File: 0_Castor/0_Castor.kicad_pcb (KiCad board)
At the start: 2 copper layers, 135.3 x 173.4 mm, 131 parts, among them U1 Nice_Nano_V2, U2 RT9701, U3 AP9101CK

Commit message: feat: add controller, battery jack, battery switch and reset switch placement
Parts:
- removed U2: RT9701, Package_TO_SOT_SMD:TO-252-4
- removed U3: AP9101CK, Package_TO_SOT_SMD:SOT-23-5
- added J1: Conn_01x02, Connector_JST:JST_PH_S2B-PH-K_1x02_P2.00mm_Horizontal, F.Cu at (135.5, 54.8)
- added R1: Resistor, ScottoKeebs_Components:Resistor_0402, F.Cu at (167.2, 125.9)
- added R2: Resistor, ScottoKeebs_Components:Resistor_0402, F.Cu at (51.9, 62.7)
- added R3: Resistor, ScottoKeebs_Components:Resistor_0402, F.Cu at (51.8, 119.8)
- added R4: Resistor, ScottoKeebs_Components:Resistor_0402, F.Cu at (156.8, 195.2)
- added SW1: Reset Switch, Button_Switch_SMD:Panasonic_EVQPUL_EVQPUC, F.Cu at (168.6, 157.4)
- added SW2: Battery Switch, footprints:SPDT_C128955, B.Cu at (170.1, 72.1)
- U1: moved to B.Cu
- moved U1 201.1 mm to (153.7, 45.3), turned to 90 degrees
- moved D63 4.58 mm to (129.2, 44.0)
- moved LED41 0.87 mm to (119.5, 166.2)
- moved S69 0.87 mm to (115.8, 180.0)
- moved LED44 0.87 mm to (151.4, 194.5)
- moved D68 0.87 mm to (128.1, 163.6)
- moved D69 0.87 mm to (123.2, 182.0)
- moved D76 0.87 mm to (146.5, 168.5)
- moved D77 0.87 mm to (141.6, 186.9)
- moved S68 0.87 mm to (120.7, 161.6)
- moved S77 0.87 mm to (134.2, 185.0)
- moved LED42 0.87 mm to (114.6, 184.6)
- moved LED43 0.87 mm to (133.0, 189.6)
- moved D83 0.87 mm to (164.9, 173.5)
- moved LED40 0.87 mm to (137.9, 171.2)
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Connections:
- LED1 pad 2: /LEDs/VSS -> /GND
- LED1 pad 3: /LED DIN0 -> Net-(LED1-DIN)
- LED1 pad 4: /LEDs/VDD -> /RAW
- LED10 pad 2: /LEDs/VSS -> /GND
- LED10 pad 4: /LEDs/VDD -> /RAW
- LED11 pad 2: /LEDs/VSS -> /GND
- LED11 pad 4: /LEDs/VDD -> /RAW
- LED12 pad 2: /LEDs/VSS -> /GND
- LED12 pad 4: /LEDs/VDD -> /RAW
- LED13 pad 2: /LEDs/VSS -> /GND
- LED13 pad 4: /LEDs/VDD -> /RAW
- LED14 pad 2: /LEDs/VSS -> /GND
- LED14 pad 4: /LEDs/VDD -> /RAW
- LED15 pad 2: /LEDs/VSS -> /GND
- LED15 pad 4: /LEDs/VDD -> /RAW
- LED16 pad 2: /LEDs/VSS -> /GND
- LED16 pad 4: /LEDs/VDD -> /RAW
- LED17 pad 2: /LEDs/VSS -> /GND
- LED17 pad 4: /LEDs/VDD -> /RAW
- LED18 pad 2: /LEDs/VSS -> /GND
- LED18 pad 4: /LEDs/VDD -> /RAW
- LED19 pad 2: /LEDs/VSS -> /GND
- LED19 pad 4: /LEDs/VDD -> /RAW
- LED2 pad 2: /LEDs/VSS -> /GND
- LED2 pad 4: /LEDs/VDD -> /RAW
- LED20 pad 2: /LEDs/VSS -> /GND
- LED20 pad 4: /LEDs/VDD -> /RAW
- LED21 pad 2: /LEDs/VSS -> /GND
- LED21 pad 4: /LEDs/VDD -> /RAW
- LED22 pad 2: /LEDs/VSS -> /GND
- LED22 pad 4: /LEDs/VDD -> /RAW
- LED23 pad 2: /LEDs/VSS -> /GND
- LED23 pad 4: /LEDs/VDD -> /RAW
- LED24 pad 2: /LEDs/VSS -> /GND
- LED24 pad 4: /LEDs/VDD -> /RAW
- LED25 pad 1: unconnected-(LED25-DOUT-Pad1) -> Net-(LED25-DOUT)
- LED25 pad 2: /LEDs/VSS -> /GND
- LED25 pad 4: /LEDs/VDD -> /RAW
- LED26 pad 2: /LEDs/VSS -> /GND
- LED26 pad 3: /LED DIN1 -> Net-(LED26-DIN)
- LED26 pad 4: /LEDs/VDD -> /RAW
- LED27 pad 2: /LEDs/VSS -> /GND
- LED27 pad 4: /LEDs/VDD -> /RAW
- LED28 pad 2: /LEDs/VSS -> /GND
- LED28 pad 4: /LEDs/VDD -> /RAW
- LED29 pad 2: /LEDs/VSS -> /GND
- LED29 pad 4: /LEDs/VDD -> /RAW
- LED3 pad 2: /LEDs/VSS -> /GND
- LED3 pad 4: /LEDs/VDD -> /RAW
- LED30 pad 2: /LEDs/VSS -> /GND
- LED30 pad 4: /LEDs/VDD -> /RAW
- LED31 pad 2: /LEDs/VSS -> /GND
- LED31 pad 4: /LEDs/VDD -> /RAW
- LED32 pad 2: /LEDs/VSS -> /GND
- LED32 pad 4: /LEDs/VDD -> /RAW
- LED33 pad 2: /LEDs/VSS -> /GND
- LED33 pad 4: /LEDs/VDD -> /RAW
- LED34 pad 2: /LEDs/VSS -> /GND
- LED34 pad 4: /LEDs/VDD -> /RAW
- LED35 pad 2: /LEDs/VSS -> /GND
- LED35 pad 4: /LEDs/VDD -> /RAW
- LED36 pad 2: /LEDs/VSS -> /GND
- LED36 pad 4: /LEDs/VDD -> /RAW
- LED37 pad 2: /LEDs/VSS -> /GND
- LED37 pad 4: /LEDs/VDD -> /RAW
- LED38 pad 2: /LEDs/VSS -> /GND
- LED38 pad 4: /LEDs/VDD -> /RAW
- LED39 pad 2: /LEDs/VSS -> /GND
- LED39 pad 4: /LEDs/VDD -> /RAW
- LED4 pad 2: /LEDs/VSS -> /GND
- LED4 pad 4: /LEDs/VDD -> /RAW
- LED40 pad 2: /LEDs/VSS -> /GND
- LED40 pad 4: /LEDs/VDD -> /RAW
- LED41 pad 2: /LEDs/VSS -> /GND
- LED41 pad 4: /LEDs/VDD -> /RAW
- LED42 pad 2: /LEDs/VSS -> /GND
- LED42 pad 4: /LEDs/VDD -> /RAW
- LED43 pad 2: /LEDs/VSS -> /GND
- LED43 pad 4: /LEDs/VDD -> /RAW
- LED44 pad 1: unconnected-(LED44-DOUT-Pad1) -> Net-(LED44-DOUT)
- LED44 pad 2: /LEDs/VSS -> /GND
- LED44 pad 4: /LEDs/VDD -> /RAW
- LED5 pad 2: /LEDs/VSS -> /GND
- LED5 pad 4: /LEDs/VDD -> /RAW
- LED6 pad 2: /LEDs/VSS -> /GND
- LED6 pad 4: /LEDs/VDD -> /RAW
- LED7 pad 2: /LEDs/VSS -> /GND
- LED7 pad 4: /LEDs/VDD -> /RAW
- LED8 pad 2: /LEDs/VSS -> /GND
- LED8 pad 4: /LEDs/VDD -> /RAW
- LED9 pad 2: /LEDs/VSS -> /GND
- LED9 pad 4: /LEDs/VDD -> /RAW
- U1 pad 22: unconnected-(U1-RST-Pad22) -> /RST
- U1 pad 23: unconnected-(U1-GND-Pad23) -> /GND
- U1 pad 24: unconnected-(U1-B+-Pad24) -> /RAW
- U1 pad 3: unconnected-(U1-GND-Pad3) -> /GND
- U1 pad 4: unconnected-(U1-GND-Pad4) -> /GND
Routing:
- net Net-(LED38-DOUT): track 36.9 -> 0.00 mm
- net Net-(LED31-DOUT): track 34.9 -> 0.00 mm
- net Net-(LED13-DOUT): track 26.5 -> 0.00 mm
- net Net-(LED41-DOUT): track 24.7 -> 0.00 mm
- net Net-(LED30-DOUT): track 23.7 -> 0.00 mm
- net Net-(LED24-DOUT): track 23.7 -> 0.00 mm
- net Net-(LED14-DOUT): track 23.7 -> 0.00 mm
- net Net-(LED1-DOUT): track 23.7 -> 0.00 mm
- net Net-(LED6-DOUT): track 23.1 -> 0.00 mm
- net Net-(LED19-DOUT): track 22.8 -> 0.00 mm
- net Net-(LED29-DOUT): track 16.9 -> 0.00 mm
- net Net-(LED23-DOUT): track 16.9 -> 0.00 mm
- net Net-(LED15-DOUT): track 16.9 -> 0.00 mm
- net Net-(LED10-DOUT): track 16.9 -> 0.00 mm
- net Net-(LED34-DOUT): track 16.9 -> 0.00 mm
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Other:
- board size 135.3 x 173.4 mm -> 135.3 x 172.8 mm
- board text removed: "Needs to be placed properly (sub-millimeter precision)"

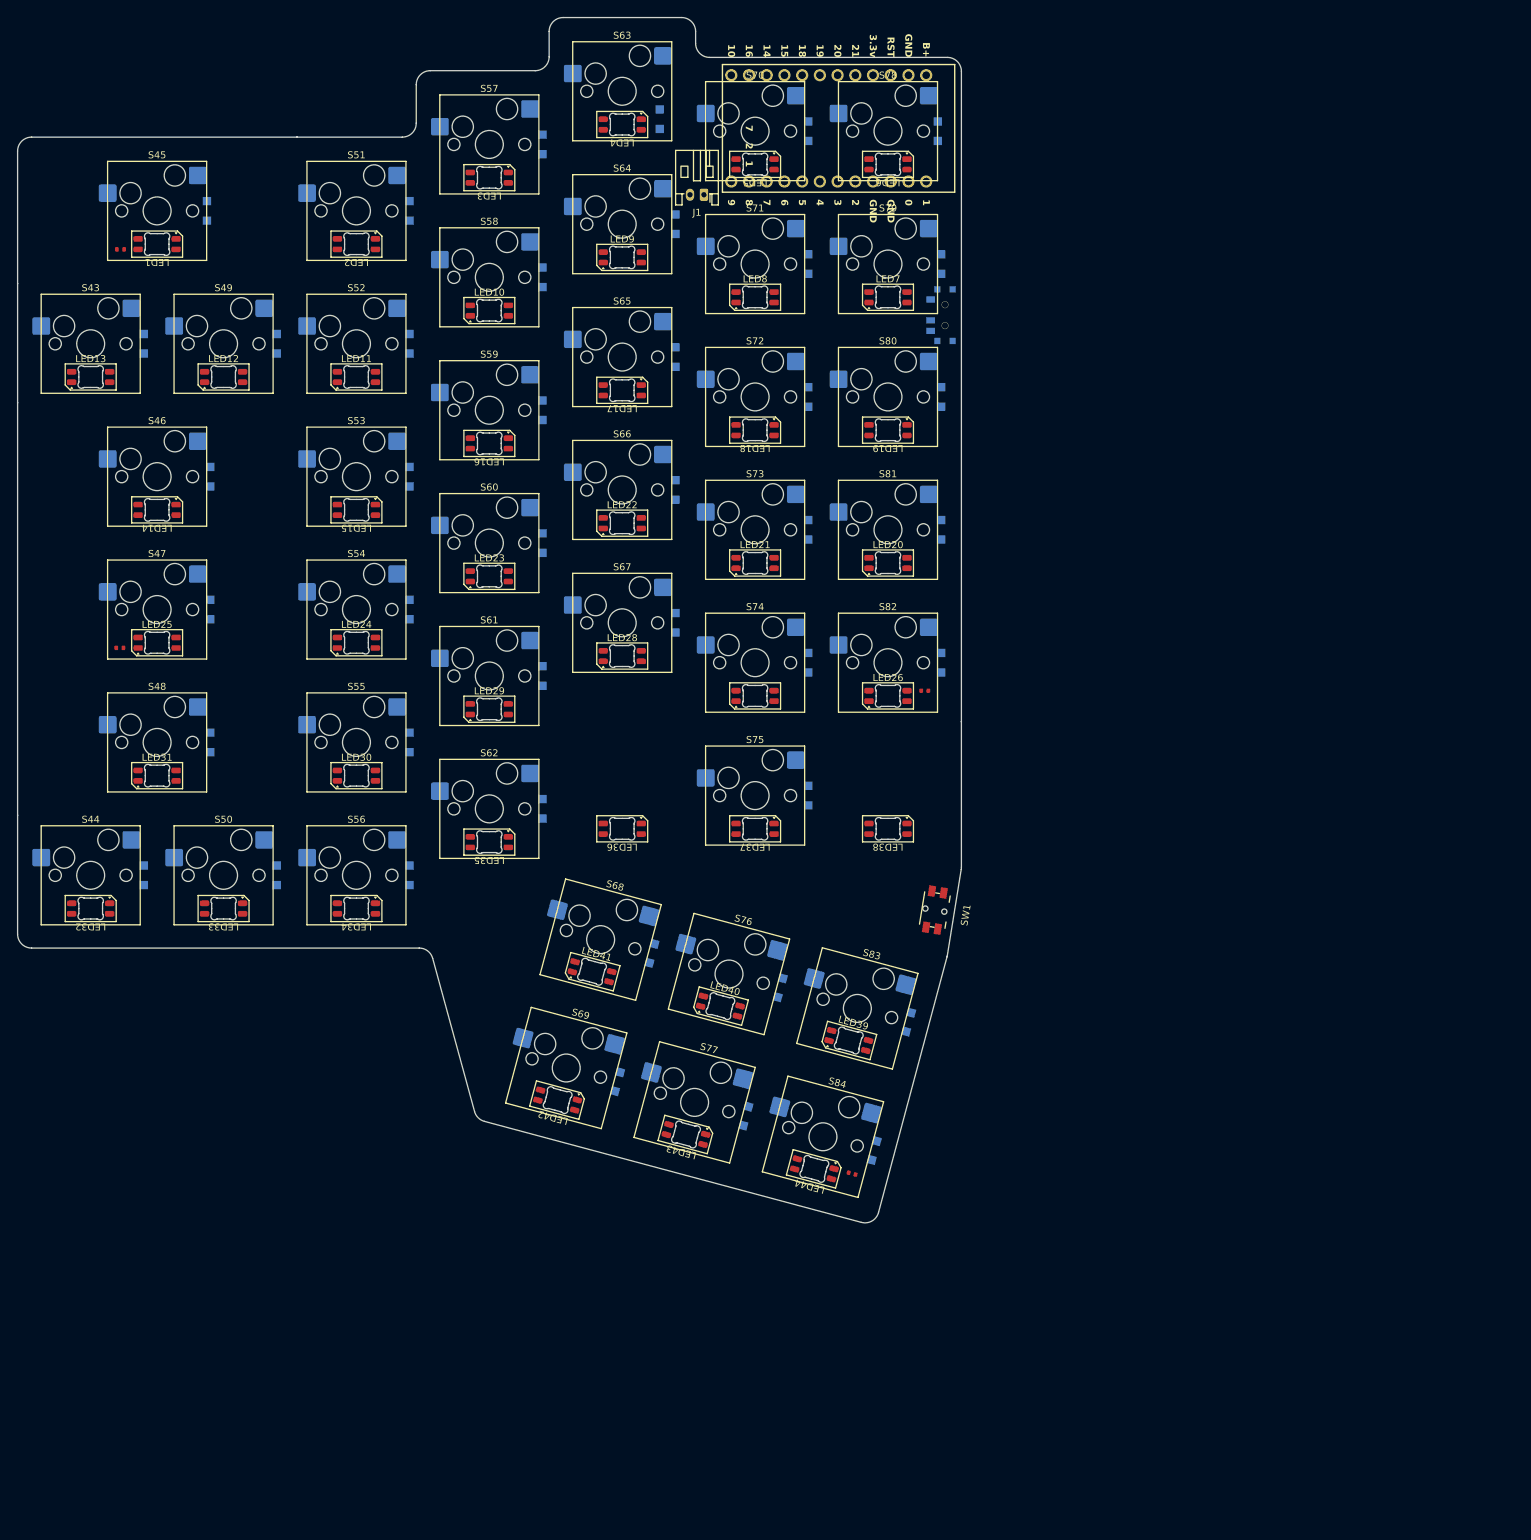
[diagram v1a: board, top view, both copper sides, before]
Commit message: feat: add LEDs, capacitors, resistors and rework schematic
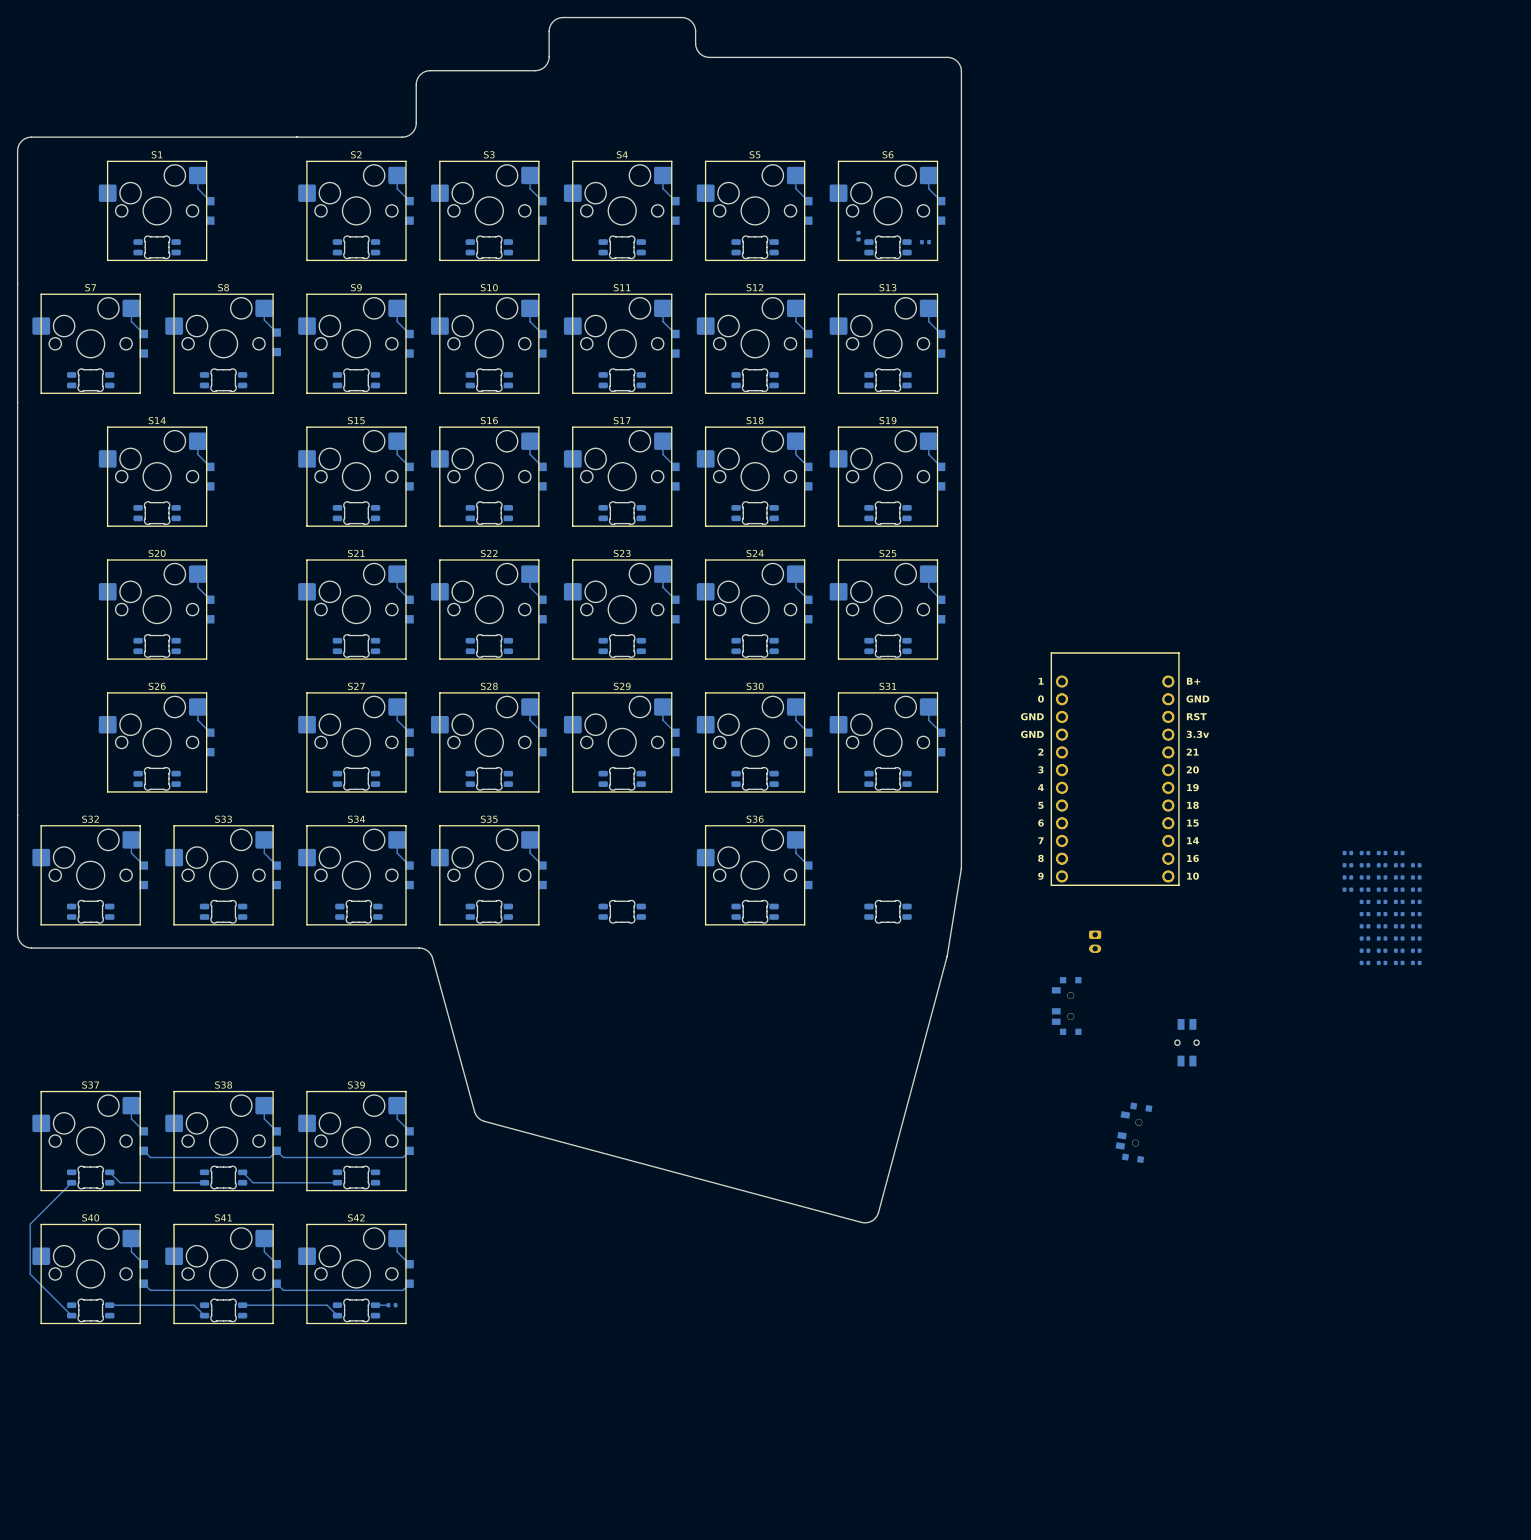
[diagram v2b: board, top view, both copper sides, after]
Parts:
- removed D43, D44, D45, D46, D47, D48, D49, D50, D51, D52, D53, D54, D55, D56, D57, D58, D59, D60, D61, D62, D63, D64, D65, D66, D67, D68, D69, D70, D71, D72, D73, D74, D75, D76, D77, D78, D79, D80, D81, D82, D83, D84: ~, Diode_SMD:Nexperia_CFP3_SOD-123W
- removed R3, R4: Resistor, ScottoKeebs_Components:Resistor_0402
- removed S43, S44, S49, S50, S51, S52, S53, S54, S55, S56, S57, S58, S59, S60, S61, S62, S63, S64, S65, S66, S67, S68, S69, S70, S71, S72, S73, S74, S76, S77, S78, S79, S80, S81, S82, S83, S84: ~, ScottoKeebs_Hotswap:Hotswap_MX_1.00u
- removed S45, S46, S47, S48: ~, ScottoKeebs_Hotswap:Hotswap_MX_2.00u
- removed S75: ~, ScottoKeebs_Hotswap:Hotswap_MX_3.00u
- added C1: 100nF, Capacitor_SMD:C_0402_1005Metric, B.Cu at (157.7, 60.8)
- added C10: 100nF, Capacitor_SMD:C_0402_1005Metric, B.Cu at (237.7, 165.0)
- added C11: 100nF, Capacitor_SMD:C_0402_1005Metric, B.Cu at (235.2, 149.2)
- added C12: 100nF, Capacitor_SMD:C_0402_1005Metric, B.Cu at (235.2, 151.0)
- added C13: 100nF, Capacitor_SMD:C_0402_1005Metric, B.Cu at (235.2, 152.7)
- added C14: 100nF, Capacitor_SMD:C_0402_1005Metric, B.Cu at (235.2, 154.5)
- added C15: 100nF, Capacitor_SMD:C_0402_1005Metric, B.Cu at (235.2, 156.2)
- added C16: 100nF, Capacitor_SMD:C_0402_1005Metric, B.Cu at (235.2, 158.0)
- added C17: 100nF, Capacitor_SMD:C_0402_1005Metric, B.Cu at (235.2, 159.7)
- added C18: 100nF, Capacitor_SMD:C_0402_1005Metric, B.Cu at (235.2, 161.5)
- added C19: 100nF, Capacitor_SMD:C_0402_1005Metric, B.Cu at (235.2, 163.2)
- added C2: 100nF, Capacitor_SMD:C_0402_1005Metric, B.Cu at (237.7, 151.0)
- added C20: 100nF, Capacitor_SMD:C_0402_1005Metric, B.Cu at (235.2, 165.0)
- added C21: 100nF, Capacitor_SMD:C_0402_1005Metric, B.Cu at (232.8, 149.2)
- added C22: 100nF, Capacitor_SMD:C_0402_1005Metric, B.Cu at (232.8, 151.0)
- added C23: 100nF, Capacitor_SMD:C_0402_1005Metric, B.Cu at (232.8, 152.7)
- added C24: 100nF, Capacitor_SMD:C_0402_1005Metric, B.Cu at (232.8, 154.5)
- added C25: 100nF, Capacitor_SMD:C_0402_1005Metric, B.Cu at (232.8, 156.2)
- added C26: 100nF, Capacitor_SMD:C_0402_1005Metric, B.Cu at (232.8, 158.0)
- added C27: 100nF, Capacitor_SMD:C_0402_1005Metric, B.Cu at (232.8, 159.7)
- added C28: 100nF, Capacitor_SMD:C_0402_1005Metric, B.Cu at (232.8, 161.5)
- added C29: 100nF, Capacitor_SMD:C_0402_1005Metric, B.Cu at (232.8, 163.2)
- added C3: 100nF, Capacitor_SMD:C_0402_1005Metric, B.Cu at (237.7, 152.7)
- added C30: 100nF, Capacitor_SMD:C_0402_1005Metric, B.Cu at (232.8, 165.0)
- added C31: 100nF, Capacitor_SMD:C_0402_1005Metric, B.Cu at (230.3, 149.2)
- added C32: 100nF, Capacitor_SMD:C_0402_1005Metric, B.Cu at (230.3, 151.0)
- added C33: 100nF, Capacitor_SMD:C_0402_1005Metric, B.Cu at (230.3, 152.7)
- added C34: 100nF, Capacitor_SMD:C_0402_1005Metric, B.Cu at (230.3, 154.5)
- added C35: 100nF, Capacitor_SMD:C_0402_1005Metric, B.Cu at (230.3, 156.2)
- added C36: 100nF, Capacitor_SMD:C_0402_1005Metric, B.Cu at (230.3, 158.0)
- added C37: 100nF, Capacitor_SMD:C_0402_1005Metric, B.Cu at (230.3, 159.7)
- added C38: 100nF, Capacitor_SMD:C_0402_1005Metric, B.Cu at (230.3, 161.5)
- added C39: 100nF, Capacitor_SMD:C_0402_1005Metric, B.Cu at (230.3, 163.2)
- added C4: 100nF, Capacitor_SMD:C_0402_1005Metric, B.Cu at (237.7, 154.5)
- added C40: 100nF, Capacitor_SMD:C_0402_1005Metric, B.Cu at (230.3, 165.0)
- added C41: 100nF, Capacitor_SMD:C_0402_1005Metric, B.Cu at (227.9, 149.2)
- added C42: 100nF, Capacitor_SMD:C_0402_1005Metric, B.Cu at (227.9, 151.0)
- added C43: 100nF, Capacitor_SMD:C_0402_1005Metric, B.Cu at (227.9, 152.7)
- added C44: 100nF, Capacitor_SMD:C_0402_1005Metric, B.Cu at (227.9, 154.5)
- added C5: 100nF, Capacitor_SMD:C_0402_1005Metric, B.Cu at (237.7, 156.2)
- added C6: 100nF, Capacitor_SMD:C_0402_1005Metric, B.Cu at (237.7, 158.0)
- added C7: 100nF, Capacitor_SMD:C_0402_1005Metric, B.Cu at (237.7, 159.7)
- added C8: 100nF, Capacitor_SMD:C_0402_1005Metric, B.Cu at (237.7, 161.5)
- added C9: 100nF, Capacitor_SMD:C_0402_1005Metric, B.Cu at (237.7, 163.2)
- added D1: ~, Diode_SMD:Nexperia_CFP3_SOD-123W, B.Cu at (64.8, 57.1)
- added D10: ~, Diode_SMD:Nexperia_CFP3_SOD-123W, B.Cu at (112.4, 76.2)
- added D11: ~, Diode_SMD:Nexperia_CFP3_SOD-123W, B.Cu at (131.4, 76.2)
- added D12: ~, Diode_SMD:Nexperia_CFP3_SOD-123W, B.Cu at (150.5, 76.2)
- added D13: ~, Diode_SMD:Nexperia_CFP3_SOD-123W, B.Cu at (169.5, 76.2)
- added D14: ~, Diode_SMD:Nexperia_CFP3_SOD-123W, B.Cu at (64.8, 95.2)
- added D15: ~, Diode_SMD:Nexperia_CFP3_SOD-123W, B.Cu at (93.3, 95.2)
- added D16: ~, Diode_SMD:Nexperia_CFP3_SOD-123W, B.Cu at (112.4, 95.2)
- added D17: ~, Diode_SMD:Nexperia_CFP3_SOD-123W, B.Cu at (131.4, 95.2)
- added D18: ~, Diode_SMD:Nexperia_CFP3_SOD-123W, B.Cu at (150.5, 95.2)
- added D19: ~, Diode_SMD:Nexperia_CFP3_SOD-123W, B.Cu at (169.5, 95.2)
- added D2: ~, Diode_SMD:Nexperia_CFP3_SOD-123W, B.Cu at (93.3, 57.1)
- added D20: ~, Diode_SMD:Nexperia_CFP3_SOD-123W, B.Cu at (64.8, 114.3)
- added D21: ~, Diode_SMD:Nexperia_CFP3_SOD-123W, B.Cu at (93.3, 114.3)
- added D22: ~, Diode_SMD:Nexperia_CFP3_SOD-123W, B.Cu at (112.4, 114.3)
- added D23: ~, Diode_SMD:Nexperia_CFP3_SOD-123W, B.Cu at (131.4, 114.3)
- added D24: ~, Diode_SMD:Nexperia_CFP3_SOD-123W, B.Cu at (150.5, 114.3)
- added D25: ~, Diode_SMD:Nexperia_CFP3_SOD-123W, B.Cu at (169.5, 114.3)
- added D26: ~, Diode_SMD:Nexperia_CFP3_SOD-123W, B.Cu at (64.8, 133.3)
- added D27: ~, Diode_SMD:Nexperia_CFP3_SOD-123W, B.Cu at (93.3, 133.3)
- added D28: ~, Diode_SMD:Nexperia_CFP3_SOD-123W, B.Cu at (112.4, 133.3)
- added D29: ~, Diode_SMD:Nexperia_CFP3_SOD-123W, B.Cu at (131.4, 133.3)
- added D3: ~, Diode_SMD:Nexperia_CFP3_SOD-123W, B.Cu at (112.4, 57.1)
- added D30: ~, Diode_SMD:Nexperia_CFP3_SOD-123W, B.Cu at (150.5, 133.3)
- added D31: ~, Diode_SMD:Nexperia_CFP3_SOD-123W, B.Cu at (169.5, 133.3)
- added D32: ~, Diode_SMD:Nexperia_CFP3_SOD-123W, B.Cu at (55.2, 152.4)
- added D33: ~, Diode_SMD:Nexperia_CFP3_SOD-123W, B.Cu at (74.3, 152.4)
- added D34: ~, Diode_SMD:Nexperia_CFP3_SOD-123W, B.Cu at (93.3, 152.4)
- added D35: ~, Diode_SMD:Nexperia_CFP3_SOD-123W, B.Cu at (112.4, 152.4)
- added D36: ~, Diode_SMD:Nexperia_CFP3_SOD-123W, B.Cu at (150.5, 152.4)
- added D37: ~, Diode_SMD:Nexperia_CFP3_SOD-123W, B.Cu at (55.2, 190.5)
- added D38: ~, Diode_SMD:Nexperia_CFP3_SOD-123W, B.Cu at (74.3, 190.5)
- added D39: ~, Diode_SMD:Nexperia_CFP3_SOD-123W, B.Cu at (93.3, 190.5)
- added D4: ~, Diode_SMD:Nexperia_CFP3_SOD-123W, B.Cu at (131.4, 57.1)
- added D40: ~, Diode_SMD:Nexperia_CFP3_SOD-123W, B.Cu at (55.2, 209.6)
- added D41: ~, Diode_SMD:Nexperia_CFP3_SOD-123W, B.Cu at (74.3, 209.6)
- added D42: ~, Diode_SMD:Nexperia_CFP3_SOD-123W, B.Cu at (93.3, 209.6)
- added D5: ~, Diode_SMD:Nexperia_CFP3_SOD-123W, B.Cu at (150.5, 57.1)
- added D6: ~, Diode_SMD:Nexperia_CFP3_SOD-123W, B.Cu at (169.5, 57.1)
- added D7: ~, Diode_SMD:Nexperia_CFP3_SOD-123W, B.Cu at (55.2, 76.2)
- added D8: ~, Diode_SMD:Nexperia_CFP3_SOD-123W, B.Cu at (74.3, 76.0)
- added D9: ~, Diode_SMD:Nexperia_CFP3_SOD-123W, B.Cu at (93.3, 76.2)
- added S1: ~, ScottoKeebs_Hotswap:Hotswap_MX_2.00u, F.Cu at (57.1, 57.1)
- added S10: ~, ScottoKeebs_Hotswap:Hotswap_MX_1.00u, F.Cu at (104.8, 76.2)
- added S11: ~, ScottoKeebs_Hotswap:Hotswap_MX_1.00u, F.Cu at (123.8, 76.2)
- added S12: ~, ScottoKeebs_Hotswap:Hotswap_MX_1.00u, F.Cu at (142.9, 76.2)
- added S13: ~, ScottoKeebs_Hotswap:Hotswap_MX_1.00u, F.Cu at (161.9, 76.2)
- added S14: ~, ScottoKeebs_Hotswap:Hotswap_MX_2.00u, F.Cu at (57.1, 95.2)
- added S15: ~, ScottoKeebs_Hotswap:Hotswap_MX_1.00u, F.Cu at (85.7, 95.2)
- added S16: ~, ScottoKeebs_Hotswap:Hotswap_MX_1.00u, F.Cu at (104.8, 95.2)
- added S17: ~, ScottoKeebs_Hotswap:Hotswap_MX_1.00u, F.Cu at (123.8, 95.2)
- added S18: ~, ScottoKeebs_Hotswap:Hotswap_MX_1.00u, F.Cu at (142.9, 95.2)
- added S19: ~, ScottoKeebs_Hotswap:Hotswap_MX_1.00u, F.Cu at (161.9, 95.2)
- added S2: ~, ScottoKeebs_Hotswap:Hotswap_MX_1.00u, F.Cu at (85.7, 57.1)
- added S20: ~, ScottoKeebs_Hotswap:Hotswap_MX_2.00u, F.Cu at (57.1, 114.3)
- added S21: ~, ScottoKeebs_Hotswap:Hotswap_MX_1.00u, F.Cu at (85.7, 114.3)
- added S22: ~, ScottoKeebs_Hotswap:Hotswap_MX_1.00u, F.Cu at (104.8, 114.3)
- added S23: ~, ScottoKeebs_Hotswap:Hotswap_MX_1.00u, F.Cu at (123.8, 114.3)
- added S24: ~, ScottoKeebs_Hotswap:Hotswap_MX_1.00u, F.Cu at (142.9, 114.3)
- added S25: ~, ScottoKeebs_Hotswap:Hotswap_MX_1.00u, F.Cu at (161.9, 114.3)
- added S26: ~, ScottoKeebs_Hotswap:Hotswap_MX_2.00u, F.Cu at (57.1, 133.3)
- added S27: ~, ScottoKeebs_Hotswap:Hotswap_MX_1.00u, F.Cu at (85.7, 133.3)
- added S28: ~, ScottoKeebs_Hotswap:Hotswap_MX_1.00u, F.Cu at (104.8, 133.3)
- added S29: ~, ScottoKeebs_Hotswap:Hotswap_MX_1.00u, F.Cu at (123.8, 133.3)
- added S3: ~, ScottoKeebs_Hotswap:Hotswap_MX_1.00u, F.Cu at (104.8, 57.1)
- added S30: ~, ScottoKeebs_Hotswap:Hotswap_MX_1.00u, F.Cu at (142.9, 133.3)
- added S31: ~, ScottoKeebs_Hotswap:Hotswap_MX_1.00u, F.Cu at (161.9, 133.3)
- added S32: ~, ScottoKeebs_Hotswap:Hotswap_MX_1.00u, F.Cu at (47.6, 152.4)
- added S33: ~, ScottoKeebs_Hotswap:Hotswap_MX_1.00u, F.Cu at (66.7, 152.4)
- added S34: ~, ScottoKeebs_Hotswap:Hotswap_MX_1.00u, F.Cu at (85.7, 152.4)
- added S35: ~, ScottoKeebs_Hotswap:Hotswap_MX_1.00u, F.Cu at (104.8, 152.4)
- added S36: ~, ScottoKeebs_Hotswap:Hotswap_MX_3.00u, F.Cu at (142.9, 152.4)
- added S37: ~, ScottoKeebs_Hotswap:Hotswap_MX_1.00u, F.Cu at (47.6, 190.5)
- added S38: ~, ScottoKeebs_Hotswap:Hotswap_MX_1.00u, F.Cu at (66.7, 190.5)
- added S39: ~, ScottoKeebs_Hotswap:Hotswap_MX_1.00u, F.Cu at (85.7, 190.5)
- added S4: ~, ScottoKeebs_Hotswap:Hotswap_MX_1.00u, F.Cu at (123.8, 57.1)
- added S40: ~, ScottoKeebs_Hotswap:Hotswap_MX_1.00u, F.Cu at (47.6, 209.6)
- added S41: ~, ScottoKeebs_Hotswap:Hotswap_MX_1.00u, F.Cu at (66.7, 209.6)
- added S42: ~, ScottoKeebs_Hotswap:Hotswap_MX_1.00u, F.Cu at (85.7, 209.6)
- added S5: ~, ScottoKeebs_Hotswap:Hotswap_MX_1.00u, F.Cu at (142.9, 57.1)
- added S6: ~, ScottoKeebs_Hotswap:Hotswap_MX_1.00u, F.Cu at (161.9, 57.1)
- added S7: ~, ScottoKeebs_Hotswap:Hotswap_MX_1.00u, F.Cu at (47.6, 76.2)
- added S8: ~, ScottoKeebs_Hotswap:Hotswap_MX_1.00u, F.Cu at (66.7, 76.2)
- added S9: ~, ScottoKeebs_Hotswap:Hotswap_MX_1.00u, F.Cu at (85.7, 76.2)
- added SW3: Reset Switch, Button_Switch_SMD:Panasonic_EVQPUL_EVQPUC, B.Cu at (204.8, 176.4)
- J1: moved to B.Cu
- LED1, LED10, LED11, LED12, LED13, LED14, LED15, LED16, LED17, LED18, LED19, LED2, LED20, LED21, LED22, LED23, LED24, LED25, LED26, LED27, LED28, LED29, LED3, LED30, LED31, LED32, LED33, LED34, LED35, LED36, LED37, LED38, LED39, LED4, LED40, LED41, LED42, LED43, LED44, LED5, LED6, LED7, LED8, LED9: value SK6812MINI -> SK6812MINI-E; moved to B.Cu
- R1, R2: value Resistor -> 500Ω; footprint ScottoKeebs_Components:Resistor_0402 -> Resistor_SMD:R_0402_1005Metric; moved to B.Cu
- SW1: value Reset Switch -> Battery Switch; footprint Button_Switch_SMD:Panasonic_EVQPUL_EVQPUC -> davidphilipbarr:SPDT_C128955; moved to B.Cu
- SW2: value Battery Switch -> LED Switch; footprint footprints:SPDT_C128955 -> davidphilipbarr:SPDT_C128955
- U1: moved to F.Cu
- moved R2 156.3 mm to (90.8, 214.0)
- moved J1 120.0 mm to (191.6, 160.9), turned to -90 degrees
- moved LED7 114.9 mm to (47.6, 81.4)
- moved LED13 114.3 mm to (161.9, 81.4)
- moved LED19 105.4 mm to (57.1, 100.5)
- moved LED20 105.4 mm to (57.1, 119.5)
- moved LED6 105.4 mm to (57.1, 62.4)
- moved LED1 104.8 mm to (161.9, 62.4)
- moved LED14 104.8 mm to (161.9, 100.5)
- moved LED25 104.8 mm to (161.9, 119.5)
- moved U1 101.5 mm to (194.5, 138.3), turned to 0 degrees
- moved SW2 100.7 mm to (188.1, 171.1)
- moved LED41 77.7 mm to (47.6, 195.7), turned to 180 degrees
- moved LED8 77.1 mm to (66.7, 81.4)
- moved LED12 76.2 mm to (142.9, 81.4)
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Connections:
- J1 pad 1: /POS -> GND
- J1 pad 2: /GND -> /POS
- LED1 pad 1: Net-(LED1-DOUT) -> GND
- LED1 pad 2: /GND -> Net-(LED1-DIN)
- LED1 pad 3: Net-(LED1-DIN) -> VDD
- LED1 pad 4: /RAW -> Net-(LED1-DOUT)
- LED10 pad 1: Net-(LED10-DOUT) -> GND
- LED10 pad 2: /GND -> Net-(LED10-DIN)
- LED10 pad 3: Net-(LED10-DIN) -> VDD
- LED10 pad 4: /RAW -> Net-(LED10-DOUT)
- LED11 pad 1: Net-(LED11-DOUT) -> GND
- LED11 pad 2: /GND -> Net-(LED10-DOUT)
- LED11 pad 3: Net-(LED10-DOUT) -> VDD
- LED11 pad 4: /RAW -> Net-(LED11-DOUT)
- LED12 pad 1: Net-(LED12-DOUT) -> GND
- LED12 pad 2: /GND -> Net-(LED11-DOUT)
- LED12 pad 3: Net-(LED11-DOUT) -> VDD
- LED12 pad 4: /RAW -> Net-(LED12-DOUT)
- LED13 pad 1: Net-(LED13-DOUT) -> GND
- LED13 pad 2: /GND -> Net-(LED12-DOUT)
- LED13 pad 3: Net-(LED12-DOUT) -> VDD
- LED13 pad 4: /RAW -> Net-(LED13-DOUT)
- LED14 pad 1: Net-(LED14-DOUT) -> GND
- LED14 pad 2: /GND -> Net-(LED13-DOUT)
- LED14 pad 3: Net-(LED13-DOUT) -> VDD
- LED14 pad 4: /RAW -> Net-(LED14-DOUT)
- LED15 pad 1: Net-(LED15-DOUT) -> GND
- LED15 pad 2: /GND -> Net-(LED14-DOUT)
- LED15 pad 3: Net-(LED14-DOUT) -> VDD
- LED15 pad 4: /RAW -> Net-(LED15-DOUT)
- LED16 pad 1: Net-(LED16-DOUT) -> GND
- LED16 pad 2: /GND -> Net-(LED15-DOUT)
- LED16 pad 3: Net-(LED15-DOUT) -> VDD
- LED16 pad 4: /RAW -> Net-(LED16-DOUT)
- LED17 pad 1: Net-(LED17-DOUT) -> GND
- LED17 pad 2: /GND -> Net-(LED16-DOUT)
- LED17 pad 3: Net-(LED16-DOUT) -> VDD
- LED17 pad 4: /RAW -> Net-(LED17-DOUT)
- LED18 pad 1: Net-(LED18-DOUT) -> GND
- LED18 pad 2: /GND -> Net-(LED17-DOUT)
- LED18 pad 3: Net-(LED17-DOUT) -> VDD
- LED18 pad 4: /RAW -> Net-(LED18-DOUT)
- LED19 pad 1: Net-(LED19-DOUT) -> GND
- LED19 pad 2: /GND -> Net-(LED18-DOUT)
- LED19 pad 3: Net-(LED18-DOUT) -> VDD
- LED19 pad 4: /RAW -> Net-(LED19-DOUT)
- LED2 pad 1: Net-(LED2-DOUT) -> GND
- LED2 pad 2: /GND -> Net-(LED1-DOUT)
- LED2 pad 3: Net-(LED1-DOUT) -> VDD
- LED2 pad 4: /RAW -> Net-(LED2-DOUT)
- LED20 pad 1: Net-(LED20-DOUT) -> GND
- LED20 pad 2: /GND -> Net-(LED19-DOUT)
- LED20 pad 3: Net-(LED19-DOUT) -> VDD
- LED20 pad 4: /RAW -> Net-(LED20-DOUT)
- LED21 pad 1: Net-(LED21-DOUT) -> GND
- LED21 pad 2: /GND -> Net-(LED20-DOUT)
- LED21 pad 3: Net-(LED20-DOUT) -> VDD
- LED21 pad 4: /RAW -> Net-(LED21-DOUT)
- LED22 pad 1: Net-(LED22-DOUT) -> GND
- LED22 pad 2: /GND -> Net-(LED21-DOUT)
- LED22 pad 3: Net-(LED21-DOUT) -> VDD
- LED22 pad 4: /RAW -> Net-(LED22-DOUT)
- LED23 pad 1: Net-(LED23-DOUT) -> GND
- LED23 pad 2: /GND -> Net-(LED22-DOUT)
- LED23 pad 3: Net-(LED22-DOUT) -> VDD
- LED23 pad 4: /RAW -> Net-(LED23-DOUT)
- LED24 pad 1: Net-(LED24-DOUT) -> GND
- LED24 pad 2: /GND -> Net-(LED23-DOUT)
- LED24 pad 3: Net-(LED23-DOUT) -> VDD
- LED24 pad 4: /RAW -> Net-(LED24-DOUT)
- LED25 pad 1: Net-(LED25-DOUT) -> GND
- LED25 pad 2: /GND -> Net-(LED24-DOUT)
- LED25 pad 3: Net-(LED24-DOUT) -> VDD
- LED25 pad 4: /RAW -> Net-(LED25-DOUT)
- LED26 pad 1: Net-(LED26-DOUT) -> GND
- LED26 pad 2: /GND -> Net-(LED25-DOUT)
- LED26 pad 3: Net-(LED26-DIN) -> VDD
- LED26 pad 4: /RAW -> Net-(LED26-DOUT)
- LED27 pad 1: Net-(LED27-DOUT) -> GND
- LED27 pad 2: /GND -> Net-(LED26-DOUT)
- LED27 pad 3: Net-(LED26-DOUT) -> VDD
- LED27 pad 4: /RAW -> Net-(LED27-DOUT)
- LED28 pad 1: Net-(LED28-DOUT) -> GND
- LED28 pad 2: /GND -> Net-(LED27-DOUT)
- LED28 pad 3: Net-(LED27-DOUT) -> VDD
- LED28 pad 4: /RAW -> Net-(LED28-DOUT)
- LED29 pad 1: Net-(LED29-DOUT) -> GND
- LED29 pad 2: /GND -> Net-(LED28-DOUT)
- LED29 pad 3: Net-(LED28-DOUT) -> VDD
- LED29 pad 4: /RAW -> Net-(LED29-DOUT)
- LED3 pad 1: Net-(LED3-DOUT) -> GND
- LED3 pad 2: /GND -> Net-(LED2-DOUT)
- LED3 pad 3: Net-(LED2-DOUT) -> VDD
- LED3 pad 4: /RAW -> Net-(LED3-DOUT)
- LED30 pad 1: Net-(LED30-DOUT) -> GND
- LED30 pad 2: /GND -> Net-(LED29-DOUT)
- LED30 pad 3: Net-(LED29-DOUT) -> VDD
- LED30 pad 4: /RAW -> Net-(LED30-DOUT)
- LED31 pad 1: Net-(LED31-DOUT) -> GND
- LED31 pad 2: /GND -> Net-(LED30-DOUT)
- LED31 pad 3: Net-(LED30-DOUT) -> VDD
- LED31 pad 4: /RAW -> Net-(LED31-DOUT)
- LED32 pad 1: Net-(LED32-DOUT) -> GND
- LED32 pad 2: /GND -> Net-(LED31-DOUT)
- LED32 pad 3: Net-(LED31-DOUT) -> VDD
- LED32 pad 4: /RAW -> Net-(LED32-DOUT)
- LED33 pad 1: Net-(LED33-DOUT) -> GND
- LED33 pad 2: /GND -> Net-(LED32-DOUT)
- LED33 pad 3: Net-(LED32-DOUT) -> VDD
- LED33 pad 4: /RAW -> Net-(LED33-DOUT)
- LED34 pad 1: Net-(LED34-DOUT) -> GND
- LED34 pad 2: /GND -> Net-(LED33-DOUT)
- LED34 pad 3: Net-(LED33-DOUT) -> VDD
- LED34 pad 4: /RAW -> Net-(LED34-DOUT)
- LED35 pad 1: Net-(LED35-DOUT) -> GND
- LED35 pad 2: /GND -> Net-(LED34-DOUT)
- LED35 pad 3: Net-(LED34-DOUT) -> VDD
- LED35 pad 4: /RAW -> Net-(LED35-DOUT)
- LED36 pad 1: Net-(LED36-DOUT) -> GND
- LED36 pad 2: /GND -> Net-(LED35-DOUT)
- LED36 pad 3: Net-(LED35-DOUT) -> VDD
- LED36 pad 4: /RAW -> Net-(LED36-DOUT)
- LED37 pad 1: Net-(LED37-DOUT) -> GND
- LED37 pad 2: /GND -> Net-(LED36-DOUT)
- LED37 pad 3: Net-(LED36-DOUT) -> VDD
- LED37 pad 4: /RAW -> Net-(LED37-DOUT)
- LED38 pad 1: Net-(LED38-DOUT) -> GND
- LED38 pad 2: /GND -> Net-(LED37-DOUT)
- LED38 pad 3: Net-(LED37-DOUT) -> VDD
- LED38 pad 4: /RAW -> Net-(LED38-DOUT)
- LED39 pad 1: Net-(LED39-DOUT) -> GND
- LED39 pad 2: /GND -> Net-(LED38-DOUT)
- LED39 pad 3: Net-(LED38-DOUT) -> VDD
- LED39 pad 4: /RAW -> Net-(LED39-DOUT)
- LED4 pad 1: Net-(LED4-DOUT) -> GND
- LED4 pad 2: /GND -> Net-(LED3-DOUT)
- LED4 pad 3: Net-(LED3-DOUT) -> VDD
- LED4 pad 4: /RAW -> Net-(LED4-DOUT)
- LED40 pad 1: Net-(LED40-DOUT) -> GND
- LED40 pad 2: /GND -> Net-(LED39-DOUT)
- LED40 pad 3: Net-(LED39-DOUT) -> VDD
- LED40 pad 4: /RAW -> Net-(LED40-DOUT)
- LED41 pad 1: Net-(LED41-DOUT) -> GND
- LED41 pad 2: /GND -> Net-(LED40-DOUT)
- LED41 pad 3: Net-(LED40-DOUT) -> VDD
- LED41 pad 4: /RAW -> Net-(LED41-DOUT)
- LED42 pad 1: Net-(LED42-DOUT) -> GND
- LED42 pad 2: /GND -> Net-(LED41-DOUT)
- LED42 pad 3: Net-(LED41-DOUT) -> VDD
- LED42 pad 4: /RAW -> Net-(LED42-DOUT)
- LED43 pad 1: Net-(LED43-DOUT) -> GND
- LED43 pad 2: /GND -> Net-(LED42-DOUT)
- LED43 pad 3: Net-(LED42-DOUT) -> VDD
- LED43 pad 4: /RAW -> Net-(LED43-DOUT)
- LED44 pad 1: Net-(LED44-DOUT) -> GND
- LED44 pad 2: /GND -> Net-(LED43-DOUT)
- LED44 pad 3: Net-(LED43-DOUT) -> VDD
- LED44 pad 4: /RAW -> Net-(LED44-DOUT)
- LED5 pad 1: Net-(LED5-DOUT) -> GND
- LED5 pad 2: /GND -> Net-(LED4-DOUT)
- LED5 pad 3: Net-(LED4-DOUT) -> VDD
- LED5 pad 4: /RAW -> Net-(LED5-DOUT)
- LED6 pad 1: Net-(LED6-DOUT) -> GND
- LED6 pad 2: /GND -> Net-(LED5-DOUT)
- LED6 pad 3: Net-(LED5-DOUT) -> VDD
- LED6 pad 4: /RAW -> Net-(LED6-DOUT)
- LED7 pad 1: Net-(LED7-DOUT) -> GND
- LED7 pad 2: /GND -> Net-(LED6-DOUT)
- LED7 pad 3: Net-(LED6-DOUT) -> VDD
- LED7 pad 4: /RAW -> Net-(LED7-DOUT)
- LED8 pad 1: Net-(LED8-DOUT) -> GND
- LED8 pad 2: /GND -> Net-(LED7-DOUT)
- LED8 pad 3: Net-(LED7-DOUT) -> VDD
- LED8 pad 4: /RAW -> Net-(LED8-DOUT)
- LED9 pad 1: Net-(LED10-DIN) -> GND
- LED9 pad 2: /GND -> Net-(LED8-DOUT)
- LED9 pad 3: Net-(LED8-DOUT) -> VDD
- LED9 pad 4: /RAW -> Net-(LED10-DIN)
- R1 pad 1: /LED DIN1 -> Net-(LED1-DIN)
- R1 pad 2: Net-(LED26-DIN) -> /LED IN
- R2 pad 1: /LED DIN0 -> Net-(LED44-DOUT)
- R2 pad 2: Net-(LED1-DIN) -> GND
- SW1 pad 1: /GND -> /POS
- SW1 pad 2: /RST -> /RAW
- SW2 pad 1: /POS -> /RAW
- SW2 pad 2: /RAW -> VDD
- U1 pad 1: /LED DIN0 -> /LED IN
- U1 pad 2: /LED DIN1 -> unconnected-(U1-0-Pad2)
- U1 pad 23: /GND -> GND
- U1 pad 3: /GND -> GND
- U1 pad 4: /GND -> GND
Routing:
- net /Row 7: track 0.00 -> 39.7 mm
- net /Row 6: track 0.00 -> 39.7 mm
- net Net-(LED41-DOUT): track 0.00 -> 24.0 mm
- net Net-(LED42-DOUT): track 0.00 -> 14.2 mm
- net Net-(LED40-DOUT): track 0.00 -> 14.2 mm
- net Net-(LED43-DOUT): track 0.00 -> 14.2 mm
- net Net-(LED39-DOUT): track 0.00 -> 14.2 mm
- net Net-(D42-A): track 0.00 -> 4.42 mm
- net Net-(D41-A): track 0.00 -> 4.42 mm
- net Net-(D39-A): track 0.00 -> 4.42 mm
- net Net-(D38-A): track 0.00 -> 4.42 mm
- net Net-(D34-A): track 0.00 -> 4.42 mm
- net Net-(D33-A): track 0.00 -> 4.42 mm
- net Net-(D21-A): track 0.00 -> 4.42 mm
- net Net-(D40-A): track 0.00 -> 4.42 mm
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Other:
- board text added: "Castor"
